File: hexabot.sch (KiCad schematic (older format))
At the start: 102 parts, among them P1 BATTERY, P10 BUMP2, P11 USB_B, P12 DEBUG, P13 NC, P14 MOTOR_R, P15 MOTOR_L, P16 UART1_5V, P17 ENC1, P18 ENC2, P19 ENC3, P2 EXT_POWER, P20 ENC4, P21 UART2_FTDI3V3, P22 NC, P23 START, P24 DYNAMIXEL2, P25 NC, P26 NC, P27 NC, P3 SERVO1, P4 SERVO2, P5 DYNAMIXEL1, P6 PICKIT, P7 PANIC BUTTON, P8 NC, P9 BUMP1, Q1 Q_NMOS_GSD, Q2 Q_NMOS_GSD, Q3 Q_NMOS_GSD, Q4 Q_NMOS_GSD, SW1 PUSH1, SW2 PUSH2, U1 PTN78020 +5V, U2 PTN78020 SERVO, U3 MCP1727, U4 DSPIC33EP256MU806, Y1 8M

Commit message: Draft layout with files
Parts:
- C1, C10, C11, C12, C13, C14, C15, C2, C26, C3, C6, C7, C8, C9, R1, R10, R11, R12, R13, R14, R15, R16, R17, R18, R19, R2, R20, R21, R22, R23, R24, R25, R26, R27, R28, R3, R35, R4, R5, R6, R7, R8, R9: footprint hexabot:R_0805_HandSoldering -> Resistors_SMD:R_0805
- D1: footprint (none) -> hexabot:SOD-128
- D10, D4, D5, D6, D7, D8, D9: footprint (none) -> Resistors_SMD:R_0805
- D2, D3: footprint (none) -> Diodes_SMD:SOD-323
- F1: footprint (none) -> Resistors_SMD:R_1206_HandSoldering
- MH1, MH2, MH3, MH4: footprint (none) -> hexabot:M3-hole-plated
- P1, P14, P15, P2, P7: footprint (none) -> Sockets_MOLEX_KK-System:Socket_MOLEX-KK-RM3-96mm_Lock_2pin_straight
- P24, P5: footprint (none) -> Pin_Headers:Pin_Header_Straight_1x03
- Q1, Q2, Q3, Q4: footprint Housings_SOT-23_SOT-143_TSOT-6:SOT-23_Handsoldering -> Housings_SOT-23_SOT-143_TSOT-6:SOT-23
- SW1, SW2: footprint (none) -> hexabot:SW_PUSH-SMD
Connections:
- net MOTOR_L_OUT_1: now also P15.2 (P2); no longer P15.1 (P1)
- net MOTOR_L_OUT_2: now also P15.1 (P1); no longer P15.2 (P2)
- net MOTOR_R_OUT_1: now also P14.2 (P2); no longer P14.1 (P1)
- net MOTOR_R_OUT_2: now also P14.1 (P1); no longer P14.2 (P2)
- net SCL: now also P22.3 (P3), R26.2; no longer P22.2 (P2), R27.1
- net SDA: now also P22.2 (P2), R27.1; no longer P22.3 (P3), R26.2

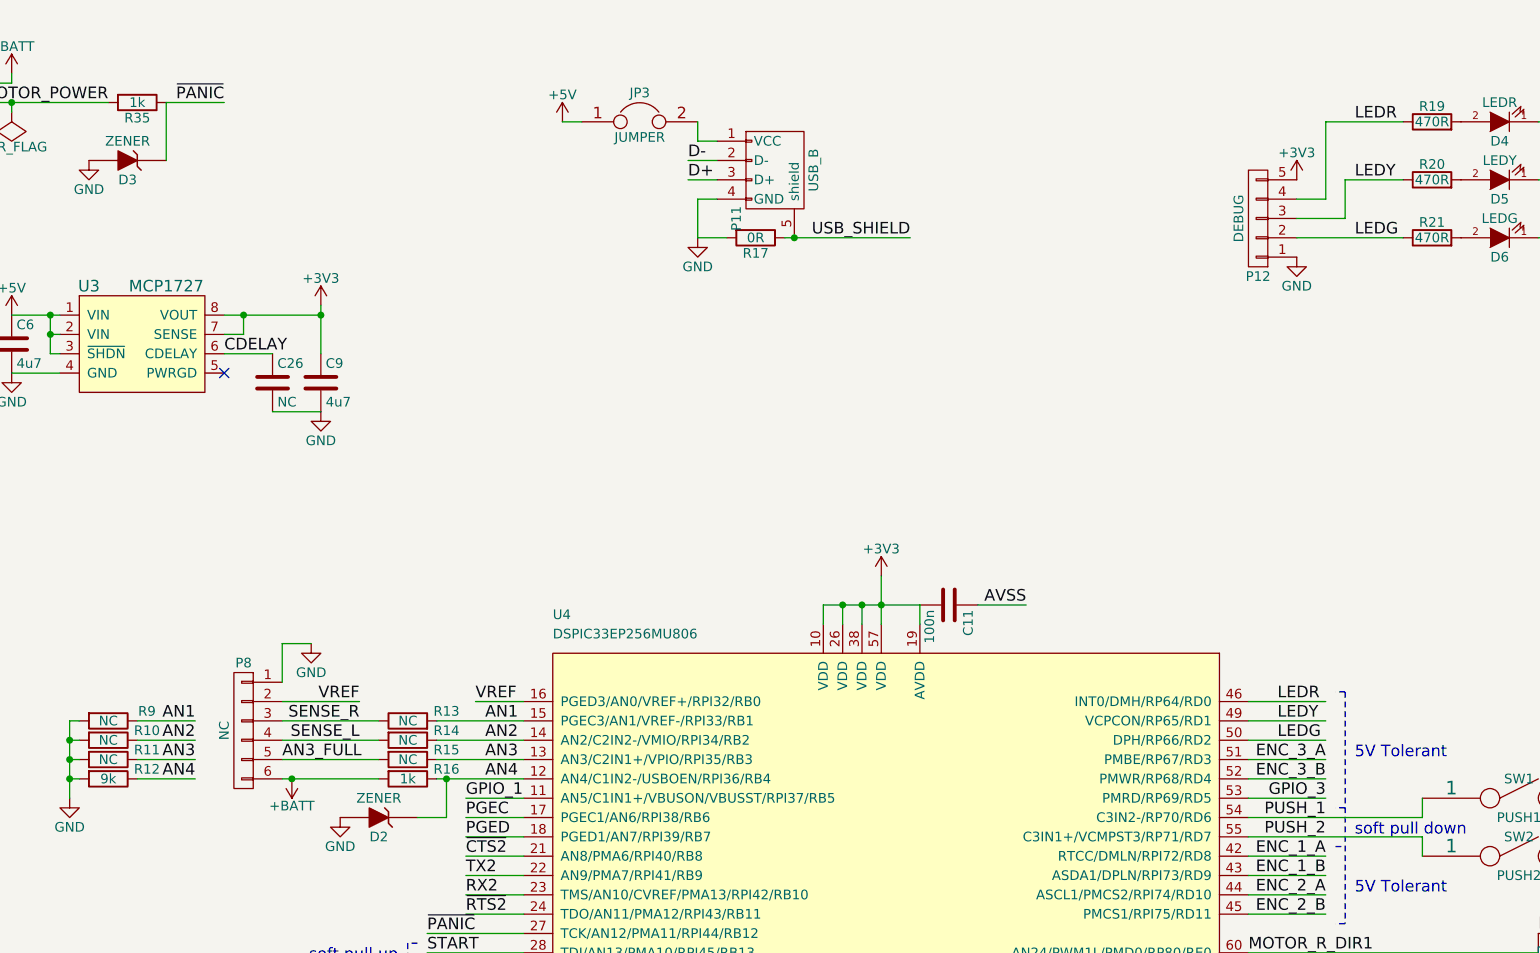
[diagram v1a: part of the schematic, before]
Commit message: Layout nearly done, ground plane to check, missing connections, change quartz footprint
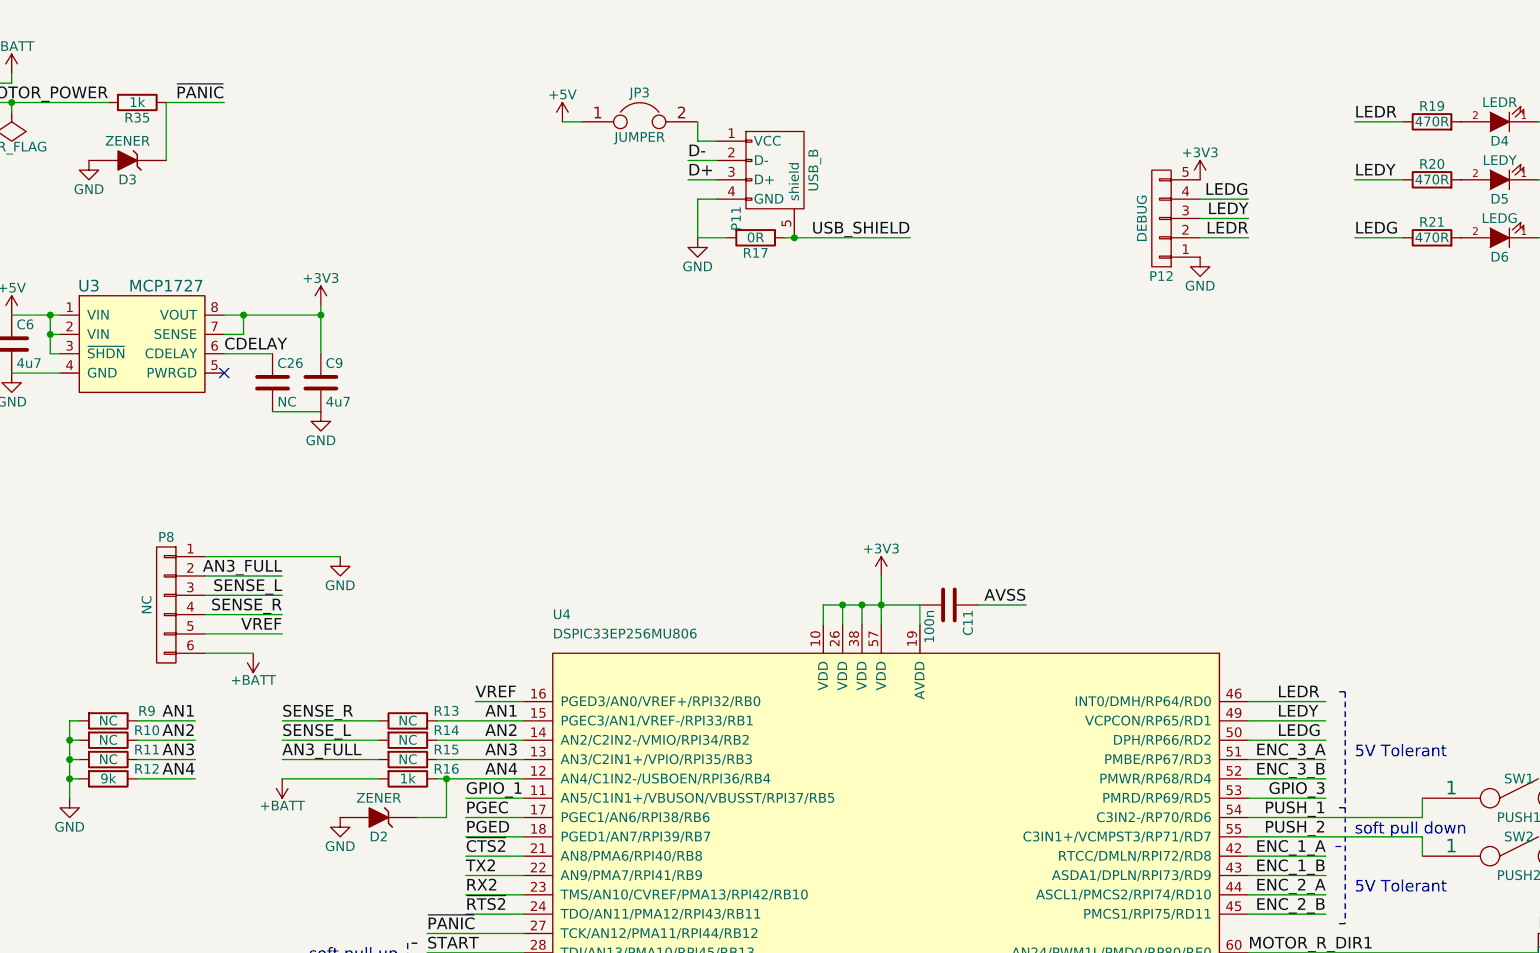
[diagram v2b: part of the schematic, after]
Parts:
- P24, P5: footprint Pin_Headers:Pin_Header_Straight_1x03 -> hexabot:molex-22-03-5035
- Y1: footprint hexabot:Crystal_HC49-SD_SMD -> Crystals:Crystal_FOX-FE_SMD
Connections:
- net AN3_FULL: now also P8.2 (P2); no longer P8.5 (P5)
- net LEDG: now also P12.4 (P4); no longer P12.2 (P2)
- net LEDR: now also P12.2 (P2); no longer P12.4 (P4)
- net SENSE_L: now also P8.3 (P3); no longer P8.4 (P4)
- net SENSE_R: now also P8.4 (P4); no longer P8.3 (P3)
- net VREF: now also P8.5 (P5); no longer P8.2 (P2)
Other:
- moved on the sheet: P12, P8

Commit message: Layout done. Print test to do.
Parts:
- LOGO1: footprint (none) -> Symbols:Symbol_OSHW-Logo_SilkScreen
- Y1: footprint Crystals:Crystal_FOX-FE_SMD -> hexabot:XTAL_5x3.2
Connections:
- net GND: now also Y1.3 (GND), Y1.4 (GND)
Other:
- moved on the sheet: Y1
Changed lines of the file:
@@
 L Crystal Y1
 U 1 1 55763091
-P 4100 6000
-F 0 "Y1" H 4100 6150 50  0000 C CNN
-F 1 "8M" H 4100 5850 50  0000 C CNN
-F 2 "Crystals:Crystal_FOX-FE_SMD" H 4100 6000 60  0001 C CNN
-F 3 "" H 4100 6000 60  0000 C CNN
-	1    4100 6000
+P 4200 6000
+F 0 "Y1" H 4200 6150 50  0000 C CNN
+F 1 "8M" H 4200 5850 50  0000 C CNN
+F 2 "hexabot:XTAL_5x3.2" H 4200 6000 60  0001 C CNN
+F 3 "" H 4200 6000 60  0000 C CNN
+	1    4200 6000
 	0    1    1    0
 $EndComp
@@
 F 0 "LOGO1" H 11150 10875 60  0000 C CNN
 F 1 "OPEN_HARDWARE_1" H 11150 10375 60  0000 C CNN
-F 2 "" H 11150 10600 60  0001 C CNN
+F 2 "Symbols:Symbol_OSHW-Logo_SilkScreen" H 11150 10600 60  0001 C CNN
 F 3 "" H 11150 10600 60  0000 C CNN
 	1    11150 10600
@@
 	1    0    0    -1
 $EndComp
-Text Label 4500 5850 2    60   ~ 0
+Text Label 4700 5850 2    60   ~ 0
 OSC1
-Text Label 4500 6150 2    60   ~ 0
+Text Label 4700 6150 2    60   ~ 0
 OSC2
 $Comp
@@
 	1550 6750 1950 6750
 Wire Wire Line
-	3500 5850 4500 5850
-Wire Wire Line
-	3500 6150 4500 6150
+	3500 5850 4700 5850
+Wire Wire Line
+	3500 6150 4700 6150
 Wire Wire Line
 	10000 7050 9750 7050
@@
 Wire Wire Line
 	3200 6150 3050 6150
-Connection ~ 4100 6150
 Connection ~ 3700 6150
-Connection ~ 4100 5850
 Connection ~ 3700 5850
 Connection ~ 11350 1450
@@
 Text Label 9750 1550 2    60   ~ 0
 LEDG
+$Comp
+L GND #PWR077
+U 1 1 557F6AE5
+P 4500 6250
+F 0 "#PWR077" H 4500 6000 50  0001 C CNN
+F 1 "GND" H 4500 6100 50  0000 C CNN
+F 2 "" H 4500 6250 60  0000 C CNN
+F 3 "" H 4500 6250 60  0000 C CNN
+	1    4500 6250
+	1    0    0    -1
+$EndComp
+$Comp
+L GND #PWR078
+U 1 1 557F6C76
+P 3900 6250
+F 0 "#PWR078" H 3900 6000 50  0001 C CNN
+F 1 "GND" H 3900 6100 50  0000 C CNN
+F 2 "" H 3900 6250 60  0000 C CNN
+F 3 "" H 3900 6250 60  0000 C CNN
+	1    3900 6250
+	1    0    0    -1
+$EndComp
+Wire Wire Line
+	3900 6000 3900 6250
+Wire Wire Line
+	4500 6000 4500 6250
+Connection ~ 4200 5850
+Connection ~ 4200 6150
 $EndSCHEMATC
